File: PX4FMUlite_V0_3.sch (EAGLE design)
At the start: 152 parts, among them J2 DF13-4P-1.25V, J201 DF13C-6P-1.25V, J202 DF13C-6P-1.25V, J203 DF13C-6P-1.25V, J3 DF13C-4P-1.25V, J302 DF13C-4P-1.25V, J401 DF13C-4P-1.25V, J403 DF13C-7P-1.25V, J405 DF13C-4P-1.25V, J801 JST-ZH-3, J802 DF13C-3P-1.25V, M3_MOUNT1101 MOUNT-HOLE3.1MM, M3_MOUNT1102 MOUNT-HOLE3.1MM, M3_MOUNT1103 MOUNT-HOLE3.1MM, M3_MOUNT1104 MOUNT-HOLE3.1MM, U101 STM32F4X7VX, U2 MAX3051, U401 MAX3051, U903 74LVC2G240, X101 3.2x2.5 mm / 24 MHz / 15 ppm

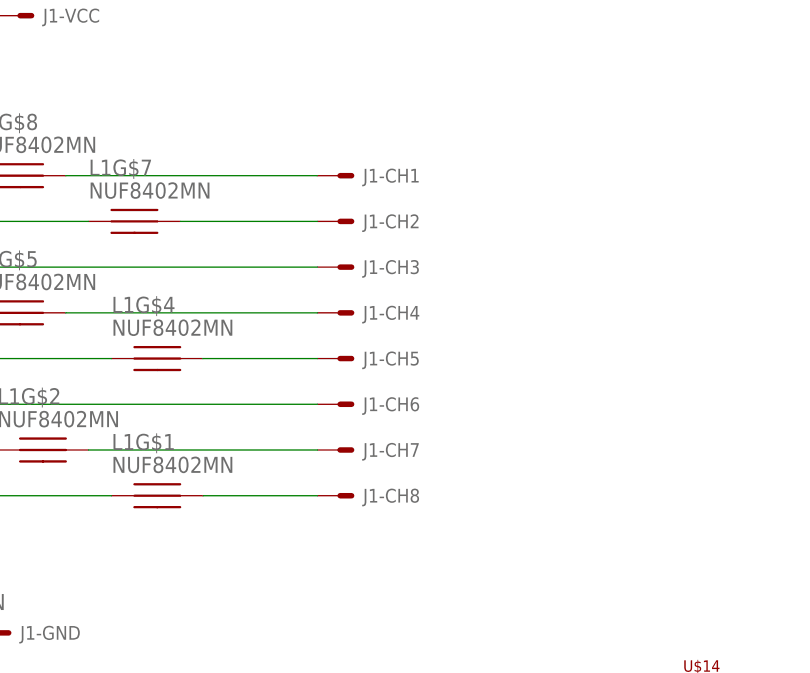
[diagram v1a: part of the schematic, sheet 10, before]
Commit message: Adjusted servo connector direction
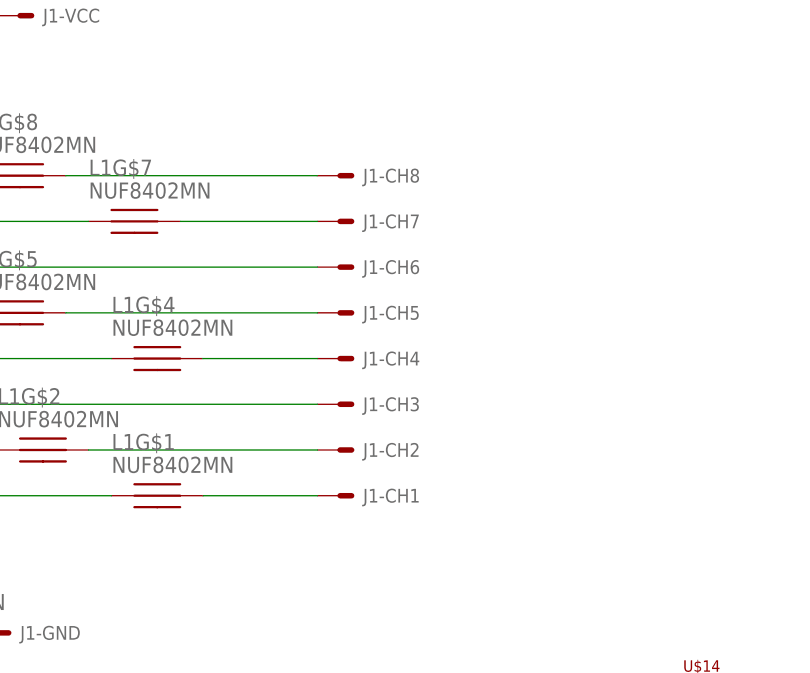
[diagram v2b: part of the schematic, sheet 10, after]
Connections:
- net FMU-CH1-PROT: now also J1-CH1.S; no longer J1-CH8.S
- net N$15: now also J1-CH8.S; no longer J1-CH1.S
- net N$16: now also J1-CH7.S; no longer J1-CH2.S
- net N$36: now also J1-CH6.S; no longer J1-CH3.S
- net N$68: now also J1-CH5.S; no longer J1-CH4.S
- net N$77: now also J1-CH4.S; no longer J1-CH5.S
- net N$78: now also J1-CH3.S; no longer J1-CH6.S
- net N$79: now also J1-CH2.S; no longer J1-CH7.S
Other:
- moved on the sheet: J1-CH1, J1-CH2, J1-CH3, J1-CH4, J1-CH5, J1-CH6, J1-CH7, J1-CH8
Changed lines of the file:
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@@
 <instance part="GND5" gate="1" x="53.34" y="78.74"/>
 <instance part="L1" gate="G$9" x="53.34" y="88.9"/>
-<instance part="J1" gate="-CH1" x="101.6" y="134.62"/>
-<instance part="J1" gate="-CH2" x="101.6" y="129.54"/>
-<instance part="J1" gate="-CH3" x="101.6" y="124.46"/>
-<instance part="J1" gate="-CH4" x="101.6" y="119.38"/>
-<instance part="J1" gate="-CH5" x="101.6" y="114.3"/>
-<instance part="J1" gate="-CH6" x="101.6" y="109.22"/>
-<instance part="J1" gate="-CH7" x="101.6" y="104.14"/>
-<instance part="J1" gate="-CH8" x="101.6" y="99.06"/>
 <instance part="J1" gate="-GND" x="63.5" y="83.82"/>
 <instance part="J1" gate="-VCC" x="66.04" y="152.4"/>
 <instance part="U$14" gate="G$1" x="142.24" y="71.12"/>
 <instance part="JP4" gate="G$1" x="165.1" y="45.72" rot="R90"/>
+<instance part="J1" gate="-CH1" x="101.6" y="99.06"/>
+<instance part="J1" gate="-CH2" x="101.6" y="104.14"/>
+<instance part="J1" gate="-CH3" x="101.6" y="109.22"/>
+<instance part="J1" gate="-CH4" x="101.6" y="114.3"/>
+<instance part="J1" gate="-CH5" x="101.6" y="119.38"/>
+<instance part="J1" gate="-CH6" x="101.6" y="124.46"/>
+<instance part="J1" gate="-CH7" x="101.6" y="129.54"/>
+<instance part="J1" gate="-CH8" x="101.6" y="134.62"/>
 </instances>
 <busses>
@@
 <wire x1="71.12" y1="119.38" x2="99.06" y2="119.38" width="0.1524" layer="91"/>
 <pinref part="L1" gate="G$5" pin="P$2"/>
-<pinref part="J1" gate="-CH4" pin="S"/>
+<pinref part="J1" gate="-CH5" pin="S"/>
 </segment>
 </net>
@@
 <pinref part="L1" gate="G$4" pin="P$2"/>
 <wire x1="86.36" y1="114.3" x2="99.06" y2="114.3" width="0.1524" layer="91"/>
-<pinref part="J1" gate="-CH5" pin="S"/>
+<pinref part="J1" gate="-CH4" pin="S"/>
 </segment>
 </net>
@@
 <pinref part="L1" gate="G$3" pin="P$2"/>
 <wire x1="58.42" y1="109.22" x2="99.06" y2="109.22" width="0.1524" layer="91"/>
-<pinref part="J1" gate="-CH6" pin="S"/>
+<pinref part="J1" gate="-CH3" pin="S"/>
 </segment>
 </net>
@@
 <pinref part="L1" gate="G$2" pin="P$2"/>
 <wire x1="73.66" y1="104.14" x2="99.06" y2="104.14" width="0.1524" layer="91"/>
-<pinref part="J1" gate="-CH7" pin="S"/>
+<pinref part="J1" gate="-CH2" pin="S"/>
 </segment>
 </net>
@@
 <pinref part="L1" gate="G$1" pin="P$2"/>
 <wire x1="86.36" y1="99.06" x2="99.06" y2="99.06" width="0.1524" layer="91"/>
-<pinref part="J1" gate="-CH8" pin="S"/>
+<pinref part="J1" gate="-CH1" pin="S"/>
 </segment>
 </net>
@@
 <pinref part="L1" gate="G$8" pin="P$2"/>
 <wire x1="71.12" y1="134.62" x2="99.06" y2="134.62" width="0.1524" layer="91"/>
-<pinref part="J1" gate="-CH1" pin="S"/>
+<pinref part="J1" gate="-CH8" pin="S"/>
 </segment>
 </net>
@@
 <wire x1="83.82" y1="129.54" x2="99.06" y2="129.54" width="0.1524" layer="91"/>
 <pinref part="L1" gate="G$7" pin="P$2"/>
-<pinref part="J1" gate="-CH2" pin="S"/>
+<pinref part="J1" gate="-CH7" pin="S"/>
 </segment>
 </net>
@@
 <pinref part="L1" gate="G$6" pin="P$2"/>
 <wire x1="58.42" y1="124.46" x2="99.06" y2="124.46" width="0.1524" layer="91"/>
-<pinref part="J1" gate="-CH3" pin="S"/>
-</segment>
-</net>
+<pinref part="J1" gate="-CH6" pin="S"/>
+</segment>
+</net>

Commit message: More wiring done
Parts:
- added C11, C12, C6: 0u1, pixhawk2:CAP0402
- added R6: 10K, pixhawk2:RESISTOR0402-RES
- C7: value 8p -> 0u1; PARTNO C1005C0G1H080C -> CC0402ZRY5V7BB104
- renumbered FMU-BOOT1101 to FMU-BOOT0, VDDA_3V1101 to VDDA_3V3_SENSORS, VDD_3V1101 to VDD_3V3
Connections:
- net N$100 renamed 5V_S3_FILTERED
- net N$101 renamed 5V_S2_FILTERED
- net N$5 renamed 5V_S1_FILTERED
- removed net VDD_5V_HIPOWER: L201.P$1
- removed net VDD_5V_IN: C10.1, C8.1, C9.1, L603.P$1, R609.2, U$15.VOUT, U$604.IN
- new net !VDD_5V_VALID: R6.1, U$15.PG
- new net N$27: C6.1, U$15.VAUX
- new net VDD_5V: C10.1, C11.1, C7.1, C8.1, C9.1, L603.P$1, R6.2, R609.2, U$15.VOUT, U$604.IN
- net GND: now also C11.2, C12.2, C6.2, C7.2, U$15.PS/SYNC
- net VDD_5V_PERIPH: now also L201.P$1
- net VDD_IN: now also C12.1
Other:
- moved on the sheet: C1, C7, C8, U$16

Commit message: Getting too tight
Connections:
- removed net !VDD_5V_HIPOWER_OC: U101PORTE_H.PE10
- removed net N$18: L1G$8.P$1
- removed net N$32: L1G$7.P$1
- new net FMU-CH6: L1G$6.P$1, U101PORTD_H.PD15
- new net FMU-CH7: L1G$7.P$1, U101PORTE_H.PE10
- net FMU-CH8: now also L1G$8.P$1; no longer L1G$6.P$1
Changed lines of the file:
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@@
 PD15: TIM4_CH4: spare
 </text>
-<text x="111.506" y="62.992" size="1.27" layer="91">Spare PWM output</text>
+<text x="129.286" y="62.992" size="1.27" layer="91">Spare PWM output</text>
 <text x="68.58" y="134.62" size="1.27" layer="91">IO debug console</text>
 <text x="112.014" y="164.592" size="1.27" layer="91">Spare ADC</text>
@@
 </segment>
 </net>
-<net name="!VDD_5V_HIPOWER_OC" class="0">
-<segment>
-<pinref part="U101" gate="PORTE_H" pin="PE10"/>
-<wire x1="175.26" y1="132.08" x2="180.34" y2="132.08" width="0.1524" layer="91"/>
-<label x="180.34" y="132.08" size="1.27" layer="95" xref="yes"/>
-</segment>
-</net>
 <net name="!FMU-LED_AMBER" class="0">
 <segment>
@@
 </segment>
 </net>
+<net name="FMU-CH6" class="0">
+<segment>
+<label x="111.76" y="63.5" size="1.27" layer="95" xref="yes"/>
+<pinref part="U101" gate="PORTD_H" pin="PD15"/>
+<wire x1="111.76" y1="63.5" x2="106.68" y2="63.5" width="0.1524" layer="91"/>
+</segment>
+</net>
+<net name="FMU-CH7" class="0">
+<segment>
+<wire x1="175.26" y1="132.08" x2="200.66" y2="132.08" width="0.1524" layer="91"/>
+<label x="200.66" y="132.08" size="2.54" layer="95" xref="yes"/>
+<pinref part="U101" gate="PORTE_H" pin="PE10"/>
+</segment>
+</net>
 </nets>
 </sheet>
@@
 </segment>
 </net>
-<net name="FMU-CH8" class="0">
-<segment>
-<wire x1="48.26" y1="124.46" x2="40.64" y2="124.46" width="0.1524" layer="91"/>
-<label x="40.64" y="124.46" size="1.27" layer="95" rot="R180" xref="yes"/>
-<label x="40.64" y="129.54" size="1.27" layer="95" rot="R180" xref="yes"/>
-<label x="40.64" y="134.62" size="1.27" layer="95" rot="R180" xref="yes"/>
-<pinref part="L1" gate="G$6" pin="P$1"/>
-</segment>
-</net>
 <net name="PPM-SBUS-PROT" class="0">
 <segment>
@@
 </segment>
 </net>
-<net name="N$32" class="0">
-<segment>
-<pinref part="L1" gate="G$7" pin="P$1"/>
-<wire x1="73.66" y1="129.54" x2="40.64" y2="129.54" width="0.1524" layer="91"/>
-</segment>
-</net>
 <net name="N$36" class="0">
 <segment>
@@
 </segment>
 </net>
-<net name="N$18" class="0">
-<segment>
-<pinref part="L1" gate="G$8" pin="P$1"/>
-<wire x1="60.96" y1="134.62" x2="40.64" y2="134.62" width="0.1524" layer="91"/>
-</segment>
-</net>
 <net name="GND" class="0">
 <segment>
@@
 </segment>
 </net>
+<net name="FMU-CH8" class="0">
+<segment>
+<wire x1="40.64" y1="134.62" x2="60.96" y2="134.62" width="0.1524" layer="91"/>
+<label x="40.64" y="134.62" size="1.27" layer="95" rot="R180" xref="yes"/>
+<pinref part="L1" gate="G$8" pin="P$1"/>
+</segment>
+</net>
+<net name="FMU-CH7" class="0">
+<segment>
+<label x="40.64" y="129.54" size="1.27" layer="95" rot="R180" xref="yes"/>
+<pinref part="L1" gate="G$7" pin="P$1"/>
+<wire x1="40.64" y1="129.54" x2="73.66" y2="129.54" width="0.1524" layer="91"/>
+</segment>
+</net>
+<net name="FMU-CH6" class="0">
+<segment>
+<wire x1="40.64" y1="124.46" x2="48.26" y2="124.46" width="0.1524" layer="91"/>
+<label x="40.64" y="124.46" size="1.27" layer="95" rot="R180" xref="yes"/>
+<pinref part="L1" gate="G$6" pin="P$1"/>
+</segment>
+</net>

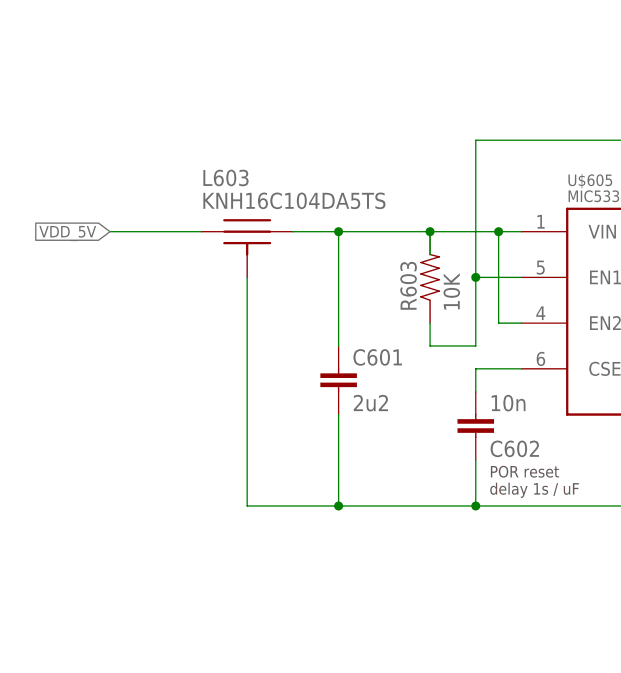
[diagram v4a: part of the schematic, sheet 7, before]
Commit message: Added FMU 3V3 LDO
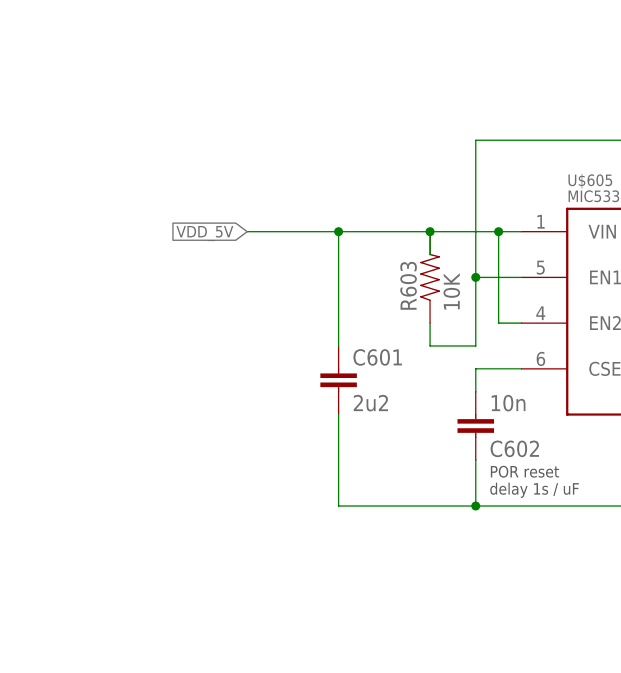
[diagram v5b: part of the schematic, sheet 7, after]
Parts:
- removed L603: KNH16C104DA5TS, pixhawk2:KNH16C104DA5TS
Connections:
- removed net FMU-VDD_5V: C1001.1, LED701.A, LED704.A, LED705.A, U$1002.VIN
- removed net FMU-VDD_5V5: C601.1, L603.P$2, R603.2, U$605.EN2, U$605.VIN
- net GND: no longer L603.P$3
- net VDD_5V: now also C1001.1, C601.1, LED701.A, LED704.A, LED705.A, R603.2, U$1002.VIN, U$605.EN2, U$605.VIN; no longer L603.P$1
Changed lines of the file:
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@@
 <attribute name="PARTNO" value="CC0402ZRY5V7BB104"/>
 </part>
-<part name="L603" library="pixhawk2" deviceset="KNH16C104DA5TS" device="">
-<attribute name="PARTNO" value="KNH16C104DA5TS"/>
-</part>
 <part name="L201" library="pixhawk2" deviceset="KNH16C104DA5TS" device="">
 <attribute name="PARTNO" value="KNH16C104DA5TS"/>
@@
 </segment>
 </net>
-<net name="VDD_5V" class="1">
-<segment>
-<pinref part="U$15" gate="A" pin="VOUT"/>
-<pinref part="C8" gate="G$1" pin="1"/>
-<wire x1="121.92" y1="121.92" x2="132.08" y2="121.92" width="0.1524" layer="91"/>
-<wire x1="132.08" y1="121.92" x2="139.7" y2="121.92" width="0.1524" layer="91"/>
-<wire x1="139.7" y1="121.92" x2="147.32" y2="121.92" width="0.1524" layer="91"/>
-<wire x1="147.32" y1="121.92" x2="157.48" y2="121.92" width="0.1524" layer="91"/>
-<wire x1="157.48" y1="121.92" x2="167.64" y2="121.92" width="0.1524" layer="91"/>
-<wire x1="167.64" y1="121.92" x2="167.64" y2="116.84" width="0.1524" layer="91"/>
-<pinref part="C10" gate="G$1" pin="1"/>
-<wire x1="157.48" y1="116.84" x2="157.48" y2="121.92" width="0.1524" layer="91"/>
-<pinref part="C9" gate="G$1" pin="1"/>
-<wire x1="147.32" y1="116.84" x2="147.32" y2="121.92" width="0.1524" layer="91"/>
-<wire x1="167.64" y1="121.92" x2="182.88" y2="121.92" width="0.1524" layer="91"/>
-<label x="190.5" y="121.92" size="1.27" layer="95" xref="yes"/>
-<junction x="167.64" y="121.92"/>
-<junction x="147.32" y="121.92"/>
-<junction x="157.48" y="121.92"/>
-<pinref part="R6" gate="G$1" pin="2"/>
-<wire x1="182.88" y1="121.92" x2="190.5" y2="121.92" width="0.1524" layer="91"/>
-<wire x1="182.88" y1="116.84" x2="182.88" y2="121.92" width="0.1524" layer="91"/>
-<junction x="182.88" y="121.92"/>
-<pinref part="C7" gate="G$1" pin="1"/>
-<wire x1="139.7" y1="116.84" x2="139.7" y2="121.92" width="0.1524" layer="91"/>
-<wire x1="132.08" y1="116.84" x2="132.08" y2="121.92" width="0.1524" layer="91"/>
-<junction x="132.08" y="121.92"/>
-<junction x="139.7" y="121.92"/>
-<pinref part="C11" gate="G$1" pin="1"/>
-</segment>
-</net>
 <net name="GND" class="0">
 <segment>
@@
 </segment>
 </net>
+<net name="VDD_5V" class="1">
+<segment>
+<pinref part="U$15" gate="A" pin="VOUT"/>
+<pinref part="C8" gate="G$1" pin="1"/>
+<wire x1="121.92" y1="121.92" x2="132.08" y2="121.92" width="0.1524" layer="91"/>
+<wire x1="132.08" y1="121.92" x2="139.7" y2="121.92" width="0.1524" layer="91"/>
+<wire x1="139.7" y1="121.92" x2="147.32" y2="121.92" width="0.1524" layer="91"/>
+<wire x1="147.32" y1="121.92" x2="157.48" y2="121.92" width="0.1524" layer="91"/>
+<wire x1="157.48" y1="121.92" x2="167.64" y2="121.92" width="0.1524" layer="91"/>
+<wire x1="167.64" y1="121.92" x2="167.64" y2="116.84" width="0.1524" layer="91"/>
+<pinref part="C10" gate="G$1" pin="1"/>
+<wire x1="157.48" y1="116.84" x2="157.48" y2="121.92" width="0.1524" layer="91"/>
+<pinref part="C9" gate="G$1" pin="1"/>
+<wire x1="147.32" y1="116.84" x2="147.32" y2="121.92" width="0.1524" layer="91"/>
+<wire x1="167.64" y1="121.92" x2="182.88" y2="121.92" width="0.1524" layer="91"/>
+<label x="190.5" y="121.92" size="1.27" layer="95" xref="yes"/>
+<junction x="167.64" y="121.92"/>
+<junction x="147.32" y="121.92"/>
+<junction x="157.48" y="121.92"/>
+<pinref part="R6" gate="G$1" pin="2"/>
+<wire x1="182.88" y1="121.92" x2="190.5" y2="121.92" width="0.1524" layer="91"/>
+<wire x1="182.88" y1="116.84" x2="182.88" y2="121.92" width="0.1524" layer="91"/>
+<junction x="182.88" y="121.92"/>
+<pinref part="C7" gate="G$1" pin="1"/>
+<wire x1="139.7" y1="116.84" x2="139.7" y2="121.92" width="0.1524" layer="91"/>
+<wire x1="132.08" y1="116.84" x2="132.08" y2="121.92" width="0.1524" layer="91"/>
+<junction x="132.08" y="121.92"/>
+<junction x="139.7" y="121.92"/>
+<pinref part="C11" gate="G$1" pin="1"/>
+</segment>
+</net>
 </nets>
 </sheet>
@@
 <attribute name="PARTNO" x="134.62" y="25.4" size="1.778" layer="96" rot="R90" display="off"/>
 </instance>
-<instance part="L603" gate="G$1" x="40.64" y="132.08">
-<attribute name="PARTNO" x="40.64" y="132.08" size="1.778" layer="96" display="off"/>
-</instance>
 <instance part="U$605" gate="G$1" x="83.82" y="127">
 <attribute name="PARTNO" x="83.82" y="127" size="1.778" layer="96" display="off"/>
@@
 <junction x="101.6" y="101.6"/>
 <junction x="111.76" y="101.6"/>
-<wire x1="40.64" y1="101.6" x2="50.8" y2="101.6" width="0.1524" layer="91"/>
 <wire x1="50.8" y1="101.6" x2="66.04" y2="101.6" width="0.1524" layer="91"/>
 <junction x="66.04" y="101.6"/>
-<pinref part="L603" gate="G$1" pin="P$3"/>
-<wire x1="40.64" y1="127" x2="40.64" y2="101.6" width="0.1524" layer="91"/>
 <pinref part="C601" gate="G$1" pin="2"/>
 <wire x1="50.8" y1="111.76" x2="50.8" y2="101.6" width="0.1524" layer="91"/>
-<junction x="50.8" y="101.6"/>
 <pinref part="C604" gate="G$1" pin="2"/>
 </segment>
@@
 </segment>
 <segment>
-<wire x1="35.56" y1="132.08" x2="25.4" y2="132.08" width="0.1524" layer="91"/>
-<label x="25.4" y="132.08" size="1.27" layer="95" rot="R180" xref="yes"/>
-<pinref part="L603" gate="G$1" pin="P$1"/>
+<label x="40.64" y="132.08" size="1.27" layer="95" rot="R180" xref="yes"/>
+<pinref part="R603" gate="G$1" pin="2"/>
+<wire x1="60.96" y1="132.08" x2="68.58" y2="132.08" width="0.1524" layer="91"/>
+<wire x1="68.58" y1="132.08" x2="71.12" y2="132.08" width="0.1524" layer="91"/>
+<wire x1="68.58" y1="121.92" x2="68.58" y2="132.08" width="0.1524" layer="91"/>
+<junction x="68.58" y="132.08"/>
+<wire x1="68.58" y1="121.92" x2="71.12" y2="121.92" width="0.1524" layer="91"/>
+<pinref part="U$605" gate="G$1" pin="VIN"/>
+<pinref part="U$605" gate="G$1" pin="EN2"/>
+<wire x1="50.8" y1="132.08" x2="60.96" y2="132.08" width="0.1524" layer="91"/>
+<wire x1="60.96" y1="132.08" x2="60.96" y2="129.54" width="0.1524" layer="91"/>
+<pinref part="C601" gate="G$1" pin="1"/>
+<wire x1="50.8" y1="119.38" x2="50.8" y2="132.08" width="0.1524" layer="91"/>
+<junction x="50.8" y="132.08"/>
+<junction x="60.96" y="132.08"/>
+<wire x1="40.64" y1="132.08" x2="50.8" y2="132.08" width="0.1524" layer="91"/>
 </segment>
 <segment>
@@
 </segment>
 </net>
-<net name="FMU-VDD_5V5" class="1">
-<segment>
-<pinref part="R603" gate="G$1" pin="2"/>
-<wire x1="60.96" y1="132.08" x2="68.58" y2="132.08" width="0.1524" layer="91"/>
-<wire x1="68.58" y1="132.08" x2="71.12" y2="132.08" width="0.1524" layer="91"/>
-<wire x1="68.58" y1="121.92" x2="68.58" y2="132.08" width="0.1524" layer="91"/>
-<junction x="68.58" y="132.08"/>
-<wire x1="68.58" y1="121.92" x2="71.12" y2="121.92" width="0.1524" layer="91"/>
-<pinref part="U$605" gate="G$1" pin="VIN"/>
-<pinref part="U$605" gate="G$1" pin="EN2"/>
-<pinref part="L603" gate="G$1" pin="P$2"/>
-<wire x1="45.72" y1="132.08" x2="50.8" y2="132.08" width="0.1524" layer="91"/>
-<wire x1="50.8" y1="132.08" x2="60.96" y2="132.08" width="0.1524" layer="91"/>
-<wire x1="60.96" y1="132.08" x2="60.96" y2="129.54" width="0.1524" layer="91"/>
-<pinref part="C601" gate="G$1" pin="1"/>
-<wire x1="50.8" y1="119.38" x2="50.8" y2="132.08" width="0.1524" layer="91"/>
-<junction x="50.8" y="132.08"/>
-<junction x="60.96" y="132.08"/>
-</segment>
-</net>
 <net name="FMU-!RESET" class="0">
 <segment>
@@
 </segment>
 </net>
-<net name="FMU-VDD_5V" class="1">
+<net name="VDD_5V" class="1">
 <segment>
 <wire x1="203.2" y1="154.94" x2="203.2" y2="152.4" width="0.1524" layer="91"/>
@@
 </segment>
 </net>
-<net name="FMU-VDD_5V" class="1">
+<net name="VDD_5V" class="1">
 <segment>
 <pinref part="C1001" gate="G$1" pin="1"/>
-<wire x1="152.4" y1="119.38" x2="124.46" y2="119.38" width="0.1524" layer="91"/>
-<wire x1="124.46" y1="119.38" x2="116.84" y2="119.38" width="0.1524" layer="91"/>
+<wire x1="152.4" y1="119.38" x2="116.84" y2="119.38" width="0.1524" layer="91"/>
 <wire x1="116.84" y1="101.6" x2="116.84" y2="119.38" width="0.1524" layer="91"/>
 <pinref part="U$1002" gate="G$1" pin="VIN"/>
-<wire x1="124.46" y1="119.38" x2="124.46" y2="129.54" width="0.1524" layer="91"/>
-<junction x="124.46" y="119.38"/>
-<label x="124.46" y="129.54" size="1.27" layer="95" rot="R180" xref="yes"/>
+<wire x1="116.84" y1="119.38" x2="116.84" y2="127" width="0.1524" layer="91"/>
+<wire x1="116.84" y1="127" x2="109.22" y2="127" width="0.1524" layer="91"/>
+<junction x="116.84" y="119.38"/>
+<label x="109.22" y="127" size="1.27" layer="95" rot="R180" xref="yes"/>
 </segment>
 </net>
